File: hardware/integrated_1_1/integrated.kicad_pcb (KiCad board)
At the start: 4 copper layers, 40 x 50 mm, 84 parts, among them J1 USB4105-GF-A-120, J2 DEBUG, J3 HDMI_A_1.4, SW1 DNF, SW2 DNF, SW3 DNF, U1 TLV76733DRVx, U10 AP5725, U11 FT2404A, U2 XC6SLX9-TQG144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

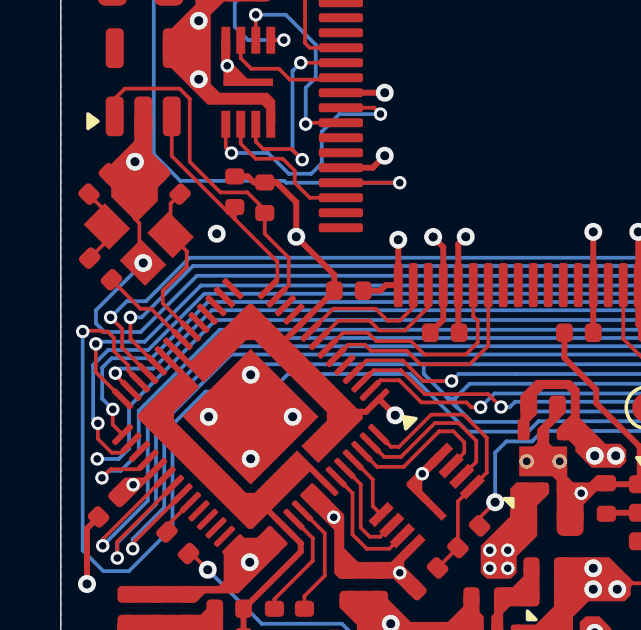
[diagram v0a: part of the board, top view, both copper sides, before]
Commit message: implemented changes as suggested by https://github.com/diminDDL
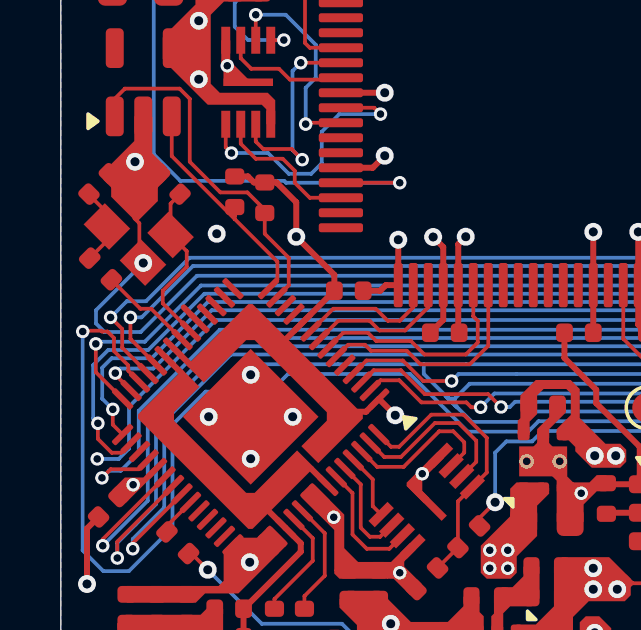
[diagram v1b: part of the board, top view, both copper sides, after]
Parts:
- R13: value 10K -> 1K
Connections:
- J1 pad S1: (no net) -> /SHIELD
- U8 pad 19: unconnected-(U8-TESTEN-Pad19) -> GND
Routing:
- net GND: track 318.9 -> 319.6 mm
